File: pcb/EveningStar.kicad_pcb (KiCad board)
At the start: 2 copper layers, 107 x 71.6 mm, 152 parts, among them J2 DEBUG, P1 WJ15EDGRC-3.81-2P, Q1 2N7002, U1 78L05G, U11 15uH, U3 ISO6721RBDR, U5 74HC14D, U6 LMR38020SDDAR, U7 ESP32-C6-WROOM-1-N8, U8 GD5F2GM7UEYIGR, U9 W5500, X1 32.768kHz, Y1 25MHz

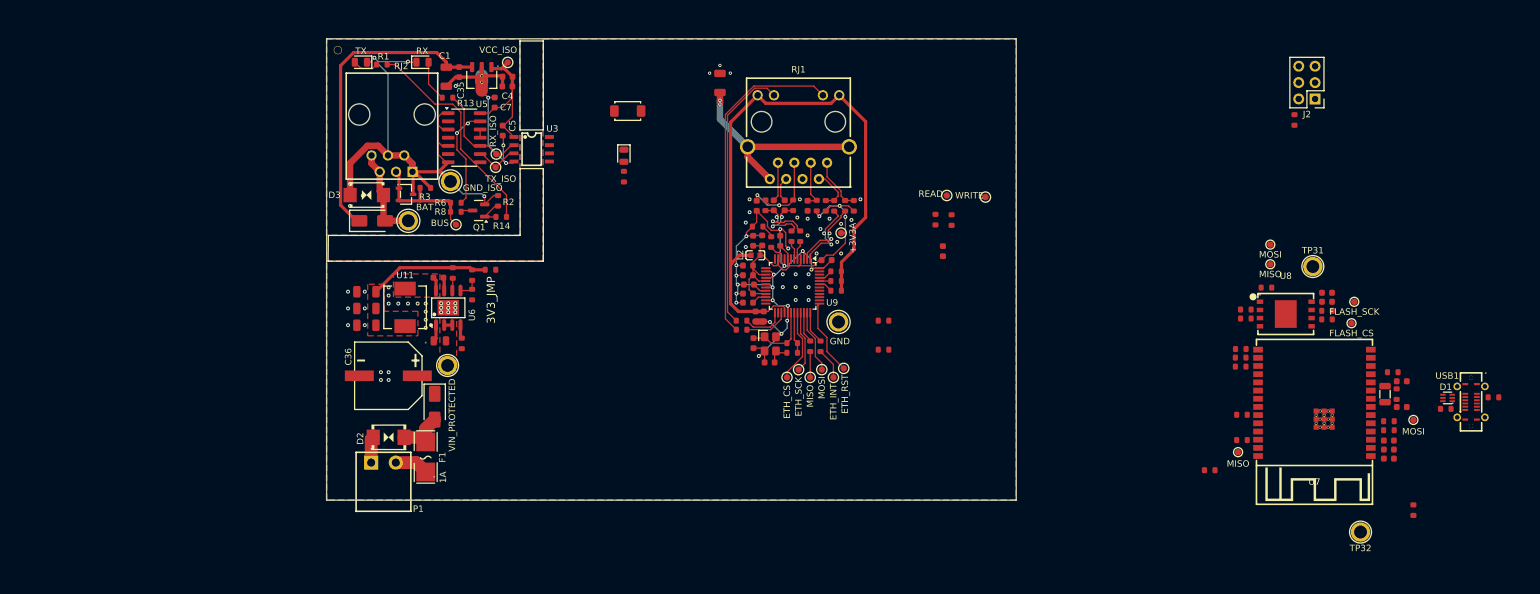
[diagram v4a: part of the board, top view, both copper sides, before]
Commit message: pcb(mcu): route most of the esp
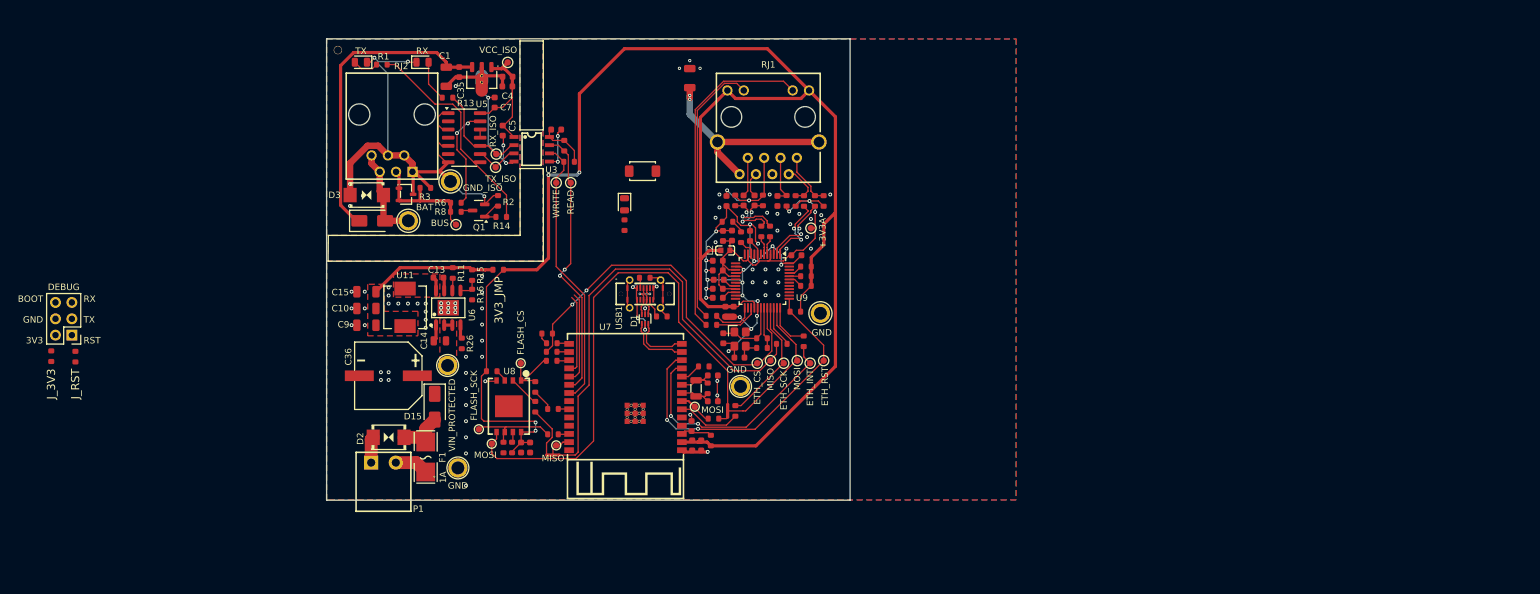
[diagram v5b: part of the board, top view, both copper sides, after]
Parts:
- removed TP30: MISO, TestPoint:TestPoint_Pad_D1.0mm
- added NT2: NetTie_3_Tee, NetTie:NetTie-3_SMD_Pad0.5mm, F.Cu at (100.6, 103.4)
- added NT3: NetTie_3_Tee, custom:NetTie-3_SMD_Pad0.5mm, F.Cu at (73.5, 110.2)
- moved J2 196.4 mm to (-1.15, 91.7)
- moved R7 196.4 mm to (-4.35, 94.9)
- moved R12 176.9 mm to (-0.60, 95.0), turned to 90 degrees
- moved TP33 137.3 mm to (62.0, 106.2), turned to 180 degrees
- moved TP31 136.3 mm to (58.8, 112.2)
- moved R18 133.0 mm to (87.7, 82.7)
- moved R66 129.3 mm to (65.8, 109.1), turned to -90 degrees
- moved USB1 129.2 mm to (87.8, 85.2), turned to 0 degrees
- moved TP15 129.0 mm to (68.5, 96.0), turned to 90 degrees
- moved R60 128.2 mm to (67.2, 109.1), turned to 90 degrees
- moved C40 127.1 mm to (68.5, 109.1), turned to 90 degrees
- moved C41 126.0 mm to (70.0, 109.1), turned to -90 degrees
- moved D1 125.1 mm to (87.8, 89.1), turned to 90 degrees
- moved TP23 124.7 mm to (64.0, 108.5)
- moved R19 122.5 mm to (90.4, 88.7), turned to 0 degrees
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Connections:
- net /usb/D+_RAW renamed /usb/D_RAW+
- net /usb/D-_RAW renamed /usb/D_RAW-
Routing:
- net +3V3: track 95.2 -> 289.1 mm, vias 0 -> 4
- net /flash/MOSI: track 0.00 -> 80.6 mm
- net /ethernet/MISO: track 4.00 -> 71.4 mm
- net /ethernet/CS: track 11.3 -> 60.0 mm, vias 0 -> 2
- net /mcu/READ: track 0.00 -> 42.9 mm, vias 0 -> 2
- net /mcu/WRITE: track 0.00 -> 42.5 mm
- net /mcu/ETH_RST: track 11.8 -> 51.9 mm, vias 0 -> 2
- net /ethernet/INT: track 4.83 -> 38.1 mm, vias 0 -> 2
- net GND: track 101.7 -> 133.5 mm, vias 75 -> 97
- net /usb/VBUS: track 0.00 -> 15.7 mm, vias 0 -> 4
- net /mcu/CFG: track 0.00 -> 14.2 mm
- net /flash/SCK: track 0.00 -> 13.8 mm
- net /ethernet/MOSI: track 9.69 -> 23.2 mm
- net /mcu/LED: track 0.00 -> 12.4 mm
- net /flash/CS: track 0.00 -> 10.9 mm
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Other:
- board size 107 x 71.6 mm -> 81.2 x 71.6 mm
- board text added: "BOOT GND 3V3"
- board text added: "RX TX RST"

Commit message: pcb: route remaining tracks
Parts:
- moved R7 96.8 mm to (88.0, 65.8), turned to 180 degrees
- moved R12 92.7 mm to (88.0, 67.8), turned to 0 degrees
- moved J2 90.4 mm to (88.0, 77.0)
- moved R22 17.9 mm to (82.3, 56.9), turned to 0 degrees
- moved S1 16.0 mm to (79.0, 79.8), turned to 90 degrees
- moved D12 15.5 mm to (79.0, 56.9), turned to 0 degrees
- moved R21 13.9 mm to (100.2, 110.0)
- moved TP29 1.61 mm to (75.4, 68.8)
- moved TP28 1.48 mm to (77.6, 68.6)
- moved R25 0.98 mm to (64.6, 82.4), turned to -90 degrees
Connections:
- U7 pad 29: (no net) -> GND
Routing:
- net /mcu/MCU_RST: track 4.85 -> 169.5 mm, vias 0 -> 2
- net /mcu/MCU_RX: track 0.00 -> 49.0 mm, vias 0 -> 6
- net /mcu/MCU_TX: track 0.00 -> 47.5 mm, vias 0 -> 8
- net /mcu/PGOOD: track 1.94 -> 46.0 mm, vias 0 -> 2
- net /mcu/LED: track 12.4 -> 56.4 mm, vias 0 -> 2
- net /mcu/BOOT9: track 1.90 -> 34.3 mm, vias 0 -> 4
- net +3V3: track 289.1 -> 317.8 mm, vias 4 -> 5
- net Net-(J2-Pin_2): track 0.00 -> 17.2 mm
- net /mcu/BOOT8: track 3.23 -> 20.3 mm
- net Net-(U6-EN): track 1.26 -> 10.4 mm
- net /mcu/CFG: track 14.2 -> 18.9 mm, vias 0 -> 2
- net /mcu/READ: track 42.9 -> 45.0 mm
- net Net-(D12-Pad2): track 0.00 -> 1.52 mm
- net GND: track 133.5 -> 134.4 mm, vias 97 -> 142
- net (no net): vias 0 -> 1

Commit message: pcb: fix most drc errors
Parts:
- TP15, TP16, TP23, TP33, TP34: footprint TestPoint:TestPoint_Pad_D1.0mm -> custom:TestPoint_Pad_D1.0mm
- TP31, TP32, TP36: footprint TestPoint:TestPoint_Plated_Hole_D2.0mm -> custom:TestPoint_Plated_Hole_D2.0mm
- X1: footprint PCM_JLCPCB:FC-135R_L3.2-W1.5 -> custom:FC-135R_L3.2-W1.5
- moved G*** 868.9 mm to (96.6, 106.5)
- moved H2 775.4 mm to (117.9, 47.4)
- moved H4 764.9 mm to (117.9, 115.4)
- moved H3 558.2 mm to (40.4, 115.4)
- moved NT3 1.47 mm to (72.5, 109.2), turned to -90 degrees
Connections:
- U7 pad 28: (no net) -> GND
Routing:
- net /ethernet/MISO: track 71.4 -> 74.0 mm
- net /flash/MISO: track 8.13 -> 6.36 mm
- net GND: track 134.4 -> 135.8 mm, vias 142 -> 143
- net (no net): vias 1 -> 0
